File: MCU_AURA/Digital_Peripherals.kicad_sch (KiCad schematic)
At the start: 20 parts, among them J300 TF-CARD_H1.8, Q300 BSS138, Q301 BSS138, Q302 BSS138, U300 ICM-20948, U301 BMP280

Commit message: Added Samacsys libraries
Made the libraries from the component search engine local.
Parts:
- J300: footprint SamacSys_Parts:TFCARDH18 -> TF-CARD_H1_8:TFCARDH18
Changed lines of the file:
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@@
 			)
 		)
-		(property "Footprint" "SamacSys_Parts:TFCARDH18"
+		(property "Footprint" "TF-CARD_H1_8:TFCARDH18"
 			(at 114.3 251.13 0)
 			(effects

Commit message: Synchronised
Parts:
- removed J300: TF-CARD_H1.8, TF-CARD_H1_8:TFCARDH18, symbol SamacSys_Parts:TF-CARD_H1.8
- added J1: TF-CARD_H1.8, TF-CARD_H1_8:TFCARDH18, symbol TF-CARD_H1_8:TF-CARD_H1.8
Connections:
- net +3V3: now also J1.4 (VDD)
- net CARD_DETECT: now also J1.CD1 (CARD_DETEC)
- net GND: now also J1.6 (VSS), J1.G1 (GND_1), J1.G2 (GND_2), J1.G3 (GND_3), J1.G4 (GND_4)
- net MISO: now also J1.7 (DAT0)
- net MOSI: now also J1.3 (CMD)
- net SCK: now also J1.5 (CLK)
- net SD_CS: now also J1.2 (CD/DAT3)
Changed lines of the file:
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@@
 	)
 	(symbol
-		(lib_id "SamacSys_Parts:TF-CARD_H1.8")
+		(lib_id "TF-CARD_H1_8:TF-CARD_H1.8")
 		(at 72.39 156.21 0)
 		(unit 1)
@@
 		(on_board yes)
 		(dnp no)
-		(property "Reference" "J300"
-			(at 79.756 146.558 0)
+		(fields_autoplaced yes)
+		(property "Reference" "J1"
+			(at 92.3133 146.05 0)
 			(effects
 				(font
@@
 			)
 		)
-		(pin "3"
+		(pin "7"
+		)
+		(pin "8"
 		)
 		(pin "5"
 		)
+		(pin "3"
+		)
+		(pin "6"
+		)
+		(pin "G1"
+		)
+		(pin "G2"
+		)
+		(pin "G3"
+		)
 		(pin "G4"
+		)
+		(pin "1"
 		)
 		(pin "CD1"
@@
 		(pin "2"
 		)
-		(pin "7"
-		)
-		(pin "8"
-		)
-		(pin "1"
-		)
 		(pin "4"
 		)
-		(pin "G3"
-		)
-		(pin "G2"
-		)
-		(pin "6"
-		)
-		(pin "G1"
-		)
 		(instances
-			(project "Summer2025"
+			(project ""
 				(path "/c0b09de1-c640-438f-9ef5-dda14a6aac71/6e3c2630-2fcb-4f90-ad6a-c196891e487c"
-					(reference "J300")
+					(reference "J1")
 					(unit 1)
 				)

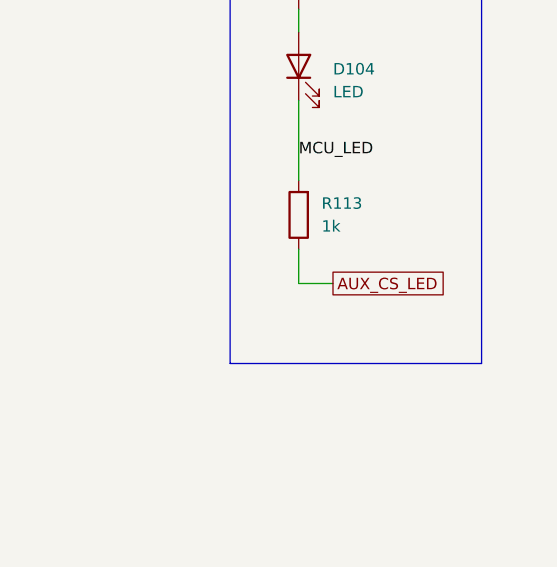
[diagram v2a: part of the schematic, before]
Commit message: Adding 3D Models
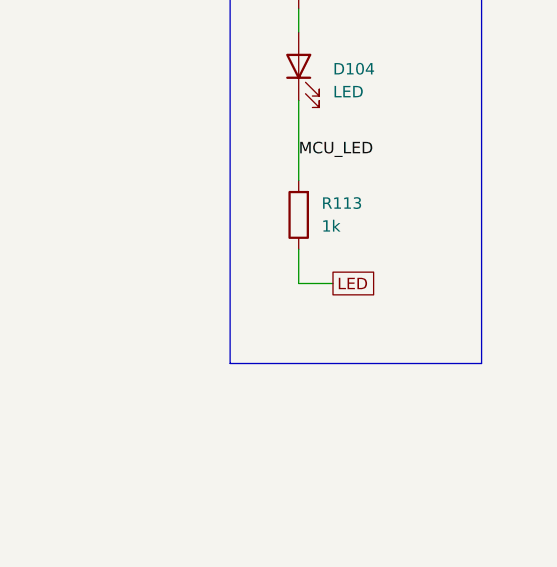
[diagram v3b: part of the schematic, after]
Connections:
- net AUX_CS_LED renamed LED
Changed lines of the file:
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@@
 		)
 	)
-	(global_label "AUX_CS_LED"
+	(global_label "LED"
 		(shape passive)
 		(at 222.25 140.97 0)
@@
 		)
 		(property "Intersheetrefs" "${INTERSHEET_REFS}"
-			(at 235.6143 140.97 0)
+			(at 227.571 140.97 0)
 			(effects
 				(font

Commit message: Adding Connectors
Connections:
- net +3V3: no longer D104.2 (A)
- net GND: now also R113.1
- net LED: now also D104.2 (A); no longer R113.1
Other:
- moved on the sheet: D104, R113
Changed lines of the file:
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@@
 	(wire
 		(pts
-			(xy 218.44 110.49) (xy 218.44 113.03)
-		)
-		(stroke
-			(width 0)
-			(type default)
-		)
-	)
-	(wire
-		(pts
 			(xy 85.09 180.34) (xy 87.63 180.34)
 		)
@@
 	(wire
 		(pts
-			(xy 222.25 140.97) (xy 218.44 140.97)
+			(xy 67.31 48.26) (xy 67.31 49.53)
 		)
 		(stroke
@@
 	(wire
 		(pts
-			(xy 67.31 48.26) (xy 67.31 49.53)
+			(xy 63.5 163.83) (xy 72.39 163.83)
 		)
 		(stroke
@@
 	(wire
 		(pts
-			(xy 63.5 163.83) (xy 72.39 163.83)
+			(xy 213.36 63.5) (xy 215.9 63.5)
 		)
 		(stroke
@@
 	(wire
 		(pts
-			(xy 213.36 63.5) (xy 215.9 63.5)
+			(xy 54.61 62.23) (xy 54.61 63.5)
 		)
 		(stroke
@@
 	(wire
 		(pts
-			(xy 54.61 62.23) (xy 54.61 63.5)
+			(xy 220.98 107.95) (xy 224.79 107.95)
 		)
 		(stroke
@@
 	(wire
 		(pts
+			(xy 220.98 107.95) (xy 220.98 113.03)
+		)
+		(stroke
+			(width 0)
+			(type default)
+		)
+	)
+	(wire
+		(pts
 			(xy 123.19 57.15) (xy 123.19 58.42)
 		)
@@
 	(wire
 		(pts
-			(xy 218.44 137.16) (xy 218.44 140.97)
+			(xy 220.98 137.16) (xy 220.98 140.97)
 		)
 		(stroke
@@
 	(wire
 		(pts
-			(xy 218.44 120.65) (xy 218.44 129.54)
+			(xy 220.98 120.65) (xy 220.98 129.54)
 		)
 		(stroke
@@
 	)
 	(label "MCU_LED"
-		(at 218.44 127 0)
+		(at 220.98 127 0)
 		(effects
 			(font
@@
 	(global_label "LED"
 		(shape passive)
-		(at 222.25 140.97 0)
+		(at 224.79 107.95 0)
 		(fields_autoplaced yes)
 		(effects
@@
 		)
 		(property "Intersheetrefs" "${INTERSHEET_REFS}"
-			(at 227.571 140.97 0)
+			(at 230.111 107.95 0)
 			(effects
 				(font
@@
 	(symbol
 		(lib_id "Device:LED")
-		(at 218.44 116.84 90)
+		(at 220.98 116.84 90)
 		(unit 1)
 		(exclude_from_sim no)
@@
 		(fields_autoplaced yes)
 		(property "Reference" "D104"
-			(at 222.25 117.1574 90)
+			(at 224.79 117.1574 90)
 			(effects
 				(font
@@
 		)
 		(property "Value" "LED"
-			(at 222.25 119.6974 90)
+			(at 224.79 119.6974 90)
 			(effects
 				(font
@@
 		)
 		(property "Footprint" "LED_SMD:LED_0603_1608Metric"
-			(at 218.44 116.84 0)
+			(at 220.98 116.84 0)
 			(effects
 				(font
@@
 		)
 		(property "Datasheet" "~"
-			(at 218.44 116.84 0)
+			(at 220.98 116.84 0)
 			(effects
 				(font
@@
 		)
 		(property "Description" "Light emitting diode"
-			(at 218.44 116.84 0)
+			(at 220.98 116.84 0)
 			(effects
 				(font
@@
 		)
 		(property "Sim.Pins" "1=K 2=A"
-			(at 218.44 116.84 0)
+			(at 220.98 116.84 0)
 			(effects
 				(font
@@
 	)
 	(symbol
-		(lib_id "power:+3V3")
-		(at 218.44 110.49 0)
-		(unit 1)
-		(exclude_from_sim no)
-		(in_bom yes)
-		(on_board yes)
-		(dnp no)
-		(fields_autoplaced yes)
-		(property "Reference" "#PWR0153"
-			(at 218.44 114.3 0)
-			(effects
-				(font
-					(size 1.27 1.27)
-				)
-				(hide yes)
-			)
-		)
-		(property "Value" "+3V3"
-			(at 218.44 105.41 0)
-			(effects
-				(font
-					(size 1.27 1.27)
-				)
-			)
-		)
-		(property "Footprint" ""
-			(at 218.44 110.49 0)
-			(effects
-				(font
-					(size 1.27 1.27)
-				)
-				(hide yes)
-			)
-		)
-		(property "Datasheet" ""
-			(at 218.44 110.49 0)
-			(effects
-				(font
-					(size 1.27 1.27)
-				)
-				(hide yes)
-			)
-		)
-		(property "Description" "Power symbol creates a global label with name \"+3V3\""
-			(at 218.44 110.49 0)
-			(effects
-				(font
-					(size 1.27 1.27)
-				)
-				(hide yes)
-			)
-		)
-		(pin "1"
-		)
-		(instances
-			(project "Summer2025"
-				(path "/c0b09de1-c640-438f-9ef5-dda14a6aac71/6e3c2630-2fcb-4f90-ad6a-c196891e487c"
-					(reference "#PWR0153")
-					(unit 1)
-				)
-			)
-		)
-	)
-	(symbol
 		(lib_id "power:+1V8")
 		(at 67.31 39.37 0)
@@
 	)
 	(symbol
+		(lib_id "power:GND")
+		(at 220.98 140.97 0)
+		(unit 1)
+		(exclude_from_sim no)
+		(in_bom yes)
+		(on_board yes)
+		(dnp no)
+		(fields_autoplaced yes)
+		(property "Reference" "#PWR022"
+			(at 220.98 147.32 0)
+			(effects
+				(font
+					(size 1.27 1.27)
+				)
+				(hide yes)
+			)
+		)
+		(property "Value" "GND"
+			(at 220.98 146.05 0)
+			(effects
+				(font
+					(size 1.27 1.27)
+				)
+				(hide yes)
+			)
+		)
+		(property "Footprint" ""
+			(at 220.98 140.97 0)
+			(effects
+				(font
+					(size 1.27 1.27)
+				)
+				(hide yes)
+			)
+		)
+		(property "Datasheet" ""
+			(at 220.98 140.97 0)
+			(effects
+				(font
+					(size 1.27 1.27)
+				)
+				(hide yes)
+			)
+		)
+		(property "Description" "Power symbol creates a global label with name \"GND\" , ground"
+			(at 220.98 140.97 0)
+			(effects
+				(font
+					(size 1.27 1.27)
+				)
+				(hide yes)
+			)
+		)
+		(pin "1"
+		)
+		(instances
+			(project "MCU_AURA"
+				(path "/c0b09de1-c640-438f-9ef5-dda14a6aac71/6e3c2630-2fcb-4f90-ad6a-c196891e487c"
+					(reference "#PWR022")
+					(unit 1)
+				)
+			)
+		)
+	)
+	(symbol
 		(lib_id "Device:R")
-		(at 218.44 133.35 180)
+		(at 220.98 133.35 180)
 		(unit 1)
 		(exclude_from_sim no)
@@
 		(fields_autoplaced yes)
 		(property "Reference" "R113"
-			(at 220.98 132.0799 0)
+			(at 223.52 132.0799 0)
 			(effects
 				(font
@@
 		)
 		(property "Value" "1k"
-			(at 220.98 134.6199 0)
+			(at 223.52 134.6199 0)
 			(effects
 				(font
@@
 		)
 		(property "Footprint" "Resistor_SMD:R_0402_1005Metric"
-			(at 220.218 133.35 90)
+			(at 222.758 133.35 90)
 			(effects
 				(font
@@
 		)
 		(property "Datasheet" "~"
-			(at 218.44 133.35 0)
+			(at 220.98 133.35 0)
 			(effects
 				(font
@@
 		)
 		(property "Description" "Resistor"
-			(at 218.44 133.35 0)
+			(at 220.98 133.35 0)
 			(effects
 				(font

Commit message: Initial Schematic Draft
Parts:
- added C303: 100n, Capacitor_SMD:C_0402_1005Metric, symbol Device:C
- added IC1: PCA9685PW,118, PCA9685PW_118:SOP65P640X110-28N, symbol PCA9685PW_118:PCA9685PW,118
- added R302: 10k, Resistor_SMD:R_0402_1005Metric, symbol Device:R
- renumbered C303 to C304, C304 to C305, C305 to C306, D104 to D300, R302 to R303, R113 to R304
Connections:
- net +3V3: now also C303.1, IC1.28 (VDD)
- net GND: now also C303.2, IC1.14 (VSS), R302.1
- net SCL: now also IC1.26 (SCL)
- net SDA: now also IC1.27 (SDA)
- new net: IC1.23 (~{OE}), R302.2
- new net SERVO_1: IC1.6 (LED0)
- new net SERVO_10: IC1.16 (LED9)
- new net SERVO_11: IC1.17 (LED10)
- new net SERVO_12: IC1.18 (LED11)
- new net SERVO_2: IC1.7 (LED1)
- new net SERVO_3: IC1.8 (LED2)
- new net SERVO_4: IC1.9 (LED3)
- new net SERVO_5: IC1.10 (LED4)
- new net SERVO_6: IC1.11 (LED5)
- new net SERVO_7: IC1.12 (LED6)
- new net SERVO_8: IC1.13 (LED7)
- new net SERVO_9: IC1.15 (LED8)
- no-connect marks 4 -> 15
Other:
- note added: "I2C address is 0x40"
- note added: "Servo Multiplexer"
- moved on the sheet: C300, C301, C302, C304, C305, C306, D300, J1, Q300, Q301, Q302, R300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

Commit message: Started Routing
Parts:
- J1: now left out of the parts list
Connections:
- net MUX_OE: now reaches IC1.23 (~{OE}), R302.2
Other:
- moved on the sheet: R302
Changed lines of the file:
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@@
 	(wire
 		(pts
-			(xy 175.26 91.44) (xy 175.26 90.17)
+			(xy 171.45 91.44) (xy 171.45 90.17)
 		)
 		(stroke
@@
 	(wire
 		(pts
-			(xy 175.26 90.17) (xy 179.07 90.17)
+			(xy 171.45 90.17) (xy 179.07 90.17)
 		)
 		(stroke
@@
 	(wire
 		(pts
-			(xy 175.26 99.06) (xy 175.26 101.6)
+			(xy 171.45 99.06) (xy 171.45 101.6)
 		)
 		(stroke
@@
 		)
 	)
+	(label "MUX_OE"
+		(at 171.45 90.17 0)
+		(effects
+			(font
+				(size 1.27 1.27)
+			)
+			(justify left bottom)
+		)
+	)
 	(global_label "LED"
 		(shape passive)
@@
 	(symbol
 		(lib_id "power:GND")
-		(at 175.26 101.6 0)
+		(at 171.45 101.6 0)
 		(unit 1)
 		(exclude_from_sim no)
@@
 		(fields_autoplaced yes)
 		(property "Reference" "#PWR06"
-			(at 175.26 107.95 0)
+			(at 171.45 107.95 0)
 			(effects
 				(font
@@
 		)
 		(property "Value" "GND"
-			(at 175.26 106.68 0)
+			(at 171.45 106.68 0)
 			(effects
 				(font
@@
 		)
 		(property "Footprint" ""
-			(at 175.26 101.6 0)
+			(at 171.45 101.6 0)
 			(effects
 				(font
@@
 		)
 		(property "Datasheet" ""
-			(at 175.26 101.6 0)
+			(at 171.45 101.6 0)
 			(effects
 				(font
@@
 		)
 		(property "Description" "Power symbol creates a global label with name \"GND\" , ground"
-			(at 175.26 101.6 0)
+			(at 171.45 101.6 0)
 			(effects
 				(font
@@
 	(symbol
 		(lib_id "Device:R")
-		(at 175.26 95.25 180)
+		(at 171.45 95.25 180)
 		(unit 1)
 		(exclude_from_sim no)
@@
 		(fields_autoplaced yes)
 		(property "Reference" "R302"
-			(at 177.8 93.9799 0)
+			(at 173.99 93.9799 0)
 			(effects
 				(font
@@
 		)
 		(property "Value" "10k"
-			(at 177.8 96.5199 0)
+			(at 173.99 96.5199 0)
 			(effects
 				(font
@@
 				)
 				(justify right)
+				(hide yes)
 			)
 		)
 		(property "Footprint" "Resistor_SMD:R_0402_1005Metric"
-			(at 177.038 95.25 90)
+			(at 173.228 95.25 90)
 			(effects
 				(font
@@
 		)
 		(property "Datasheet" "~"
-			(at 175.26 95.25 0)
+			(at 171.45 95.25 0)
 			(effects
 				(font
@@
 		)
 		(property "Description" "Resistor"
-			(at 175.26 95.25 0)
+			(at 171.45 95.25 0)
 			(effects
 				(font
@@
 		(unit 1)
 		(exclude_from_sim no)
-		(in_bom yes)
+		(in_bom no)
 		(on_board yes)
 		(dnp no)

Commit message: First fully routed version
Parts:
- added R302, R303: 10k, Resistor_SMD:R_0402_1005Metric, symbol Device:R
- C306: now not fitted; now left out of the parts list
- renumbered R302 to R304, R304 to R305, R303 to R306
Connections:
- net +1V8: now also R303.2
- net +3V3: now also R302.2
- net ICM_INT: now also R302.1
- net ICM_INT_1V8: now also R303.1
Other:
- moved on the sheet: Q302

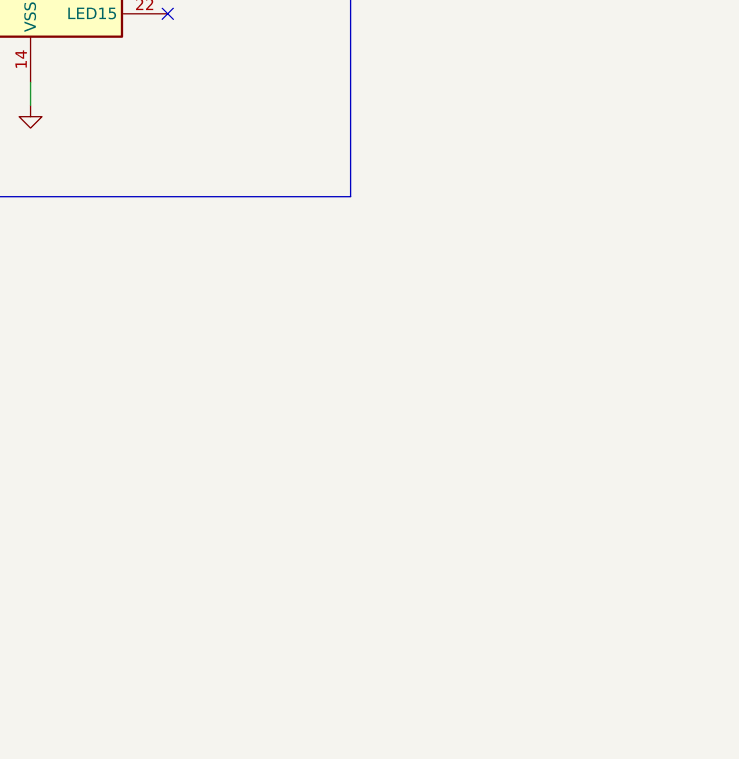
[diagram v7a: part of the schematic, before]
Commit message: Replaced JTAG with Flash
JTAG is used through USB so a Flash chip was added to MCU. PDB is just being cleaned up currently.
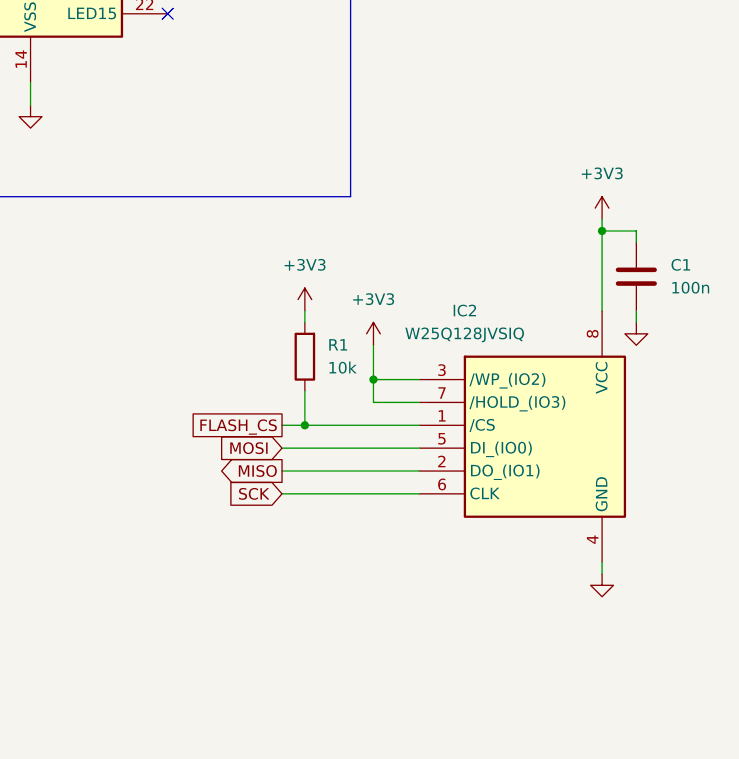
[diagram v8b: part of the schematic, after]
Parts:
- added C1: 100n, Capacitor_SMD:C_0402_1005Metric, symbol Device:C
- added IC2: W25Q128JVSIQ, SOIC127P790X216-8N, symbol W25Q128JVSIQ:W25Q128JVSIQ
- added R1: 10k, Resistor_SMD:R_0402_1005Metric, symbol Device:R
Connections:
- net +3V3: now also C1.1, IC2.3 (/WP_(IO2)), IC2.7 (/HOLD_(IO3)), IC2.8 (VCC), R1.2
- net GND: now also C1.2, IC2.4 (GND)
- net MISO: now also IC2.2 (DO_(IO1))
- net MOSI: now also IC2.5 (DI_(IO0))
- net SCK: now also IC2.6 (CLK)
- new net FLASH_CS: IC2.1 (/CS), R1.1
